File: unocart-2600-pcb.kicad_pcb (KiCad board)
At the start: 2 copper layers, 41.3 x 47.6 mm, 19 parts, among them J1 Conn_02x12_Counter_Clockwise, J2 Micro_SD_Card, J3 Conn_02x03_Odd_Even, J4 Conn_01x03, U1 STM32F407VGTx, U2 MIC5504-3.3YM5

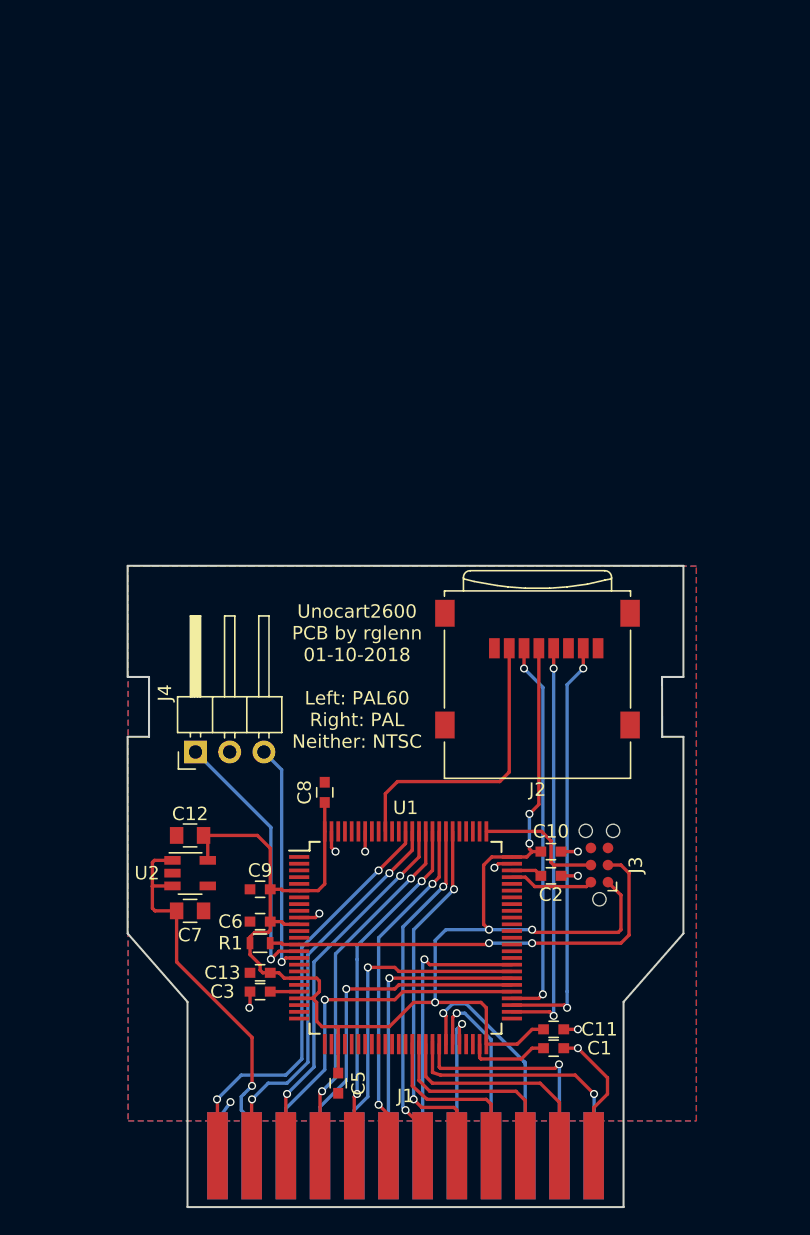
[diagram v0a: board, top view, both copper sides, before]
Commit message: Updating schematic to latest KiCAD libraries Updating PCB to add pull-up resistor on SD card DO Changing to TF-01A push/push MicroSD card socket Updating PCB size to allow a card removal slot on the cartridge body Moving parts to not conflict with internal cartridge face plate Moving PAL60/PAL jumper to solder bridges (I'm doing NTSC, I don't really care about PAL anyways)
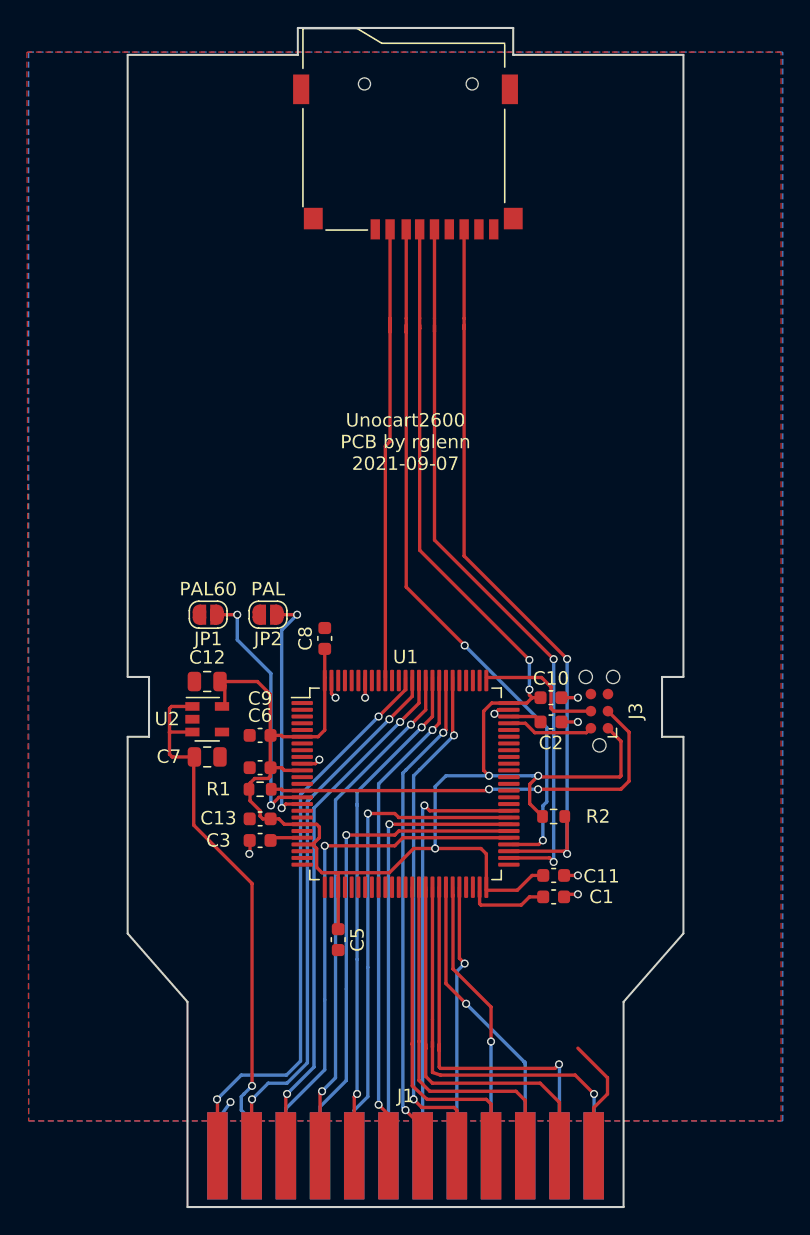
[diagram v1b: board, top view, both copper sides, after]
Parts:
- removed J4: Conn_01x03, Pin_Headers:Pin_Header_Angled_1x03_Pitch2.54mm
- added JP1: PAL60, Jumper:SolderJumper-2_P1.3mm_Open_RoundedPad1.0x1.5mm, F.Cu at (85.3, 56.0)
- added JP2: PAL, Jumper:SolderJumper-2_P1.3mm_Open_RoundedPad1.0x1.5mm, F.Cu at (89.8, 56.0)
- added R2: 10K, Resistor_SMD:R_0603_1608Metric, F.Cu at (111.0, 71.0)
- C1, C10, C11, C13, C2, C3, C5, C6, C8, C9: footprint Capacitors_SMD:C_0603 -> Capacitor_SMD:C_0603_1608Metric
- C12, C7: footprint Capacitors_SMD:C_0805 -> Capacitor_SMD:C_0805_2012Metric
- J2: footprint Connect:microSD_Card_Receptacle_Wuerth_693072010801 -> unocart-2600:microSD_HRO_TF_01A
- J3: footprint Connect:Tag-Connect_TC2030-IDC-NL -> Connector:Tag-Connect_TC2030-IDC-NL_2x03_P1.27mm_Vertical
- R1: footprint Resistors_SMD:R_0603 -> Resistor_SMD:R_0603_1608Metric
- U1: footprint Housings_QFP:LQFP-100_14x14mm_Pitch0.5mm -> Package_QFP:LQFP-100_14x14mm_P0.5mm
- U2: footprint TO_SOT_Packages_SMD:TSOT-23-5 -> Package_TO_SOT_SMD:SOT-23-5
- moved J2 42.4 mm to (100.0, 19.9), turned to 180 degrees
- moved C12 11.5 mm to (85.3, 61.0)
- moved C7 11.5 mm to (85.3, 66.6)
- moved U2 11.5 mm to (85.3, 63.8)
- moved C2 11.4 mm to (110.8, 64.0)
- moved C9 11.4 mm to (89.2, 65.0)
- moved R1 11.4 mm to (89.2, 69.0)
- moved U1 11.4 mm to (100.0, 68.6)
- moved C8 11.4 mm to (94.0, 57.8)
- moved C10 11.4 mm to (110.8, 62.2)
- moved C11 11.4 mm to (111.0, 75.4)
- moved C13 11.4 mm to (89.2, 71.2)
- moved C6 11.4 mm to (89.2, 67.4)
- moved J3 11.4 mm to (114.4, 63.2)
- moved C1 11.2 mm to (111.0, 77.0)
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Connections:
- J2 pad 1: (no net) -> Net-(J2-Pad1)
- J2 pad 8: (no net) -> Net-(J2-Pad8)
- J3 pad 6: (no net) -> Net-(J3-Pad6)
- U1 pad 1: (no net) -> Net-(U1-Pad1)
- U1 pad 12: (no net) -> Net-(U1-Pad12)
- U1 pad 13: (no net) -> Net-(U1-Pad13)
- U1 pad 17: (no net) -> Net-(U1-Pad17)
- U1 pad 18: (no net) -> Net-(U1-Pad18)
- U1 pad 2: (no net) -> Net-(U1-Pad2)
- U1 pad 23: (no net) -> Net-(U1-Pad23)
- U1 pad 24: (no net) -> Net-(U1-Pad24)
- U1 pad 25: (no net) -> Net-(U1-Pad25)
- U1 pad 26: (no net) -> Net-(U1-Pad26)
- U1 pad 29: (no net) -> Net-(U1-Pad29)
- U1 pad 3: (no net) -> Net-(U1-Pad3)
- U1 pad 30: (no net) -> Net-(U1-Pad30)
- U1 pad 31: (no net) -> Net-(U1-Pad31)
- U1 pad 32: (no net) -> Net-(U1-Pad32)
- U1 pad 33: (no net) -> Net-(U1-Pad33)
- U1 pad 34: (no net) -> Net-(U1-Pad34)
- U1 pad 35: (no net) -> Net-(U1-Pad35)
- U1 pad 36: (no net) -> Net-(U1-Pad36)
- U1 pad 37: (no net) -> Net-(U1-Pad37)
- U1 pad 38: (no net) -> Net-(U1-Pad38)
- U1 pad 4: (no net) -> Net-(U1-Pad4)
- U1 pad 47: (no net) -> Net-(U1-Pad47)
- U1 pad 48: (no net) -> Net-(U1-Pad48)
- U1 pad 5: (no net) -> Net-(U1-Pad5)
- U1 pad 51: (no net) -> Net-(U1-Pad51)
- U1 pad 60: (no net) -> Net-(U1-Pad60)
- U1 pad 61: (no net) -> Net-(U1-Pad61)
- U1 pad 62: (no net) -> Net-(U1-Pad62)
- U1 pad 63: (no net) -> Net-(U1-Pad63)
- U1 pad 64: (no net) -> Net-(U1-Pad64)
- U1 pad 65: (no net) -> Net-(U1-Pad65)
- U1 pad 66: (no net) -> Net-(U1-Pad66)
- U1 pad 67: (no net) -> Net-(U1-Pad67)
- U1 pad 68: (no net) -> Net-(U1-Pad68)
- U1 pad 69: (no net) -> Net-(U1-Pad69)
- U1 pad 7: (no net) -> Net-(U1-Pad7)
- U1 pad 70: (no net) -> Net-(U1-Pad70)
- U1 pad 71: (no net) -> Net-(U1-Pad71)
- U1 pad 77: (no net) -> Net-(U1-Pad77)
- U1 pad 78: (no net) -> Net-(U1-Pad78)
- U1 pad 79: (no net) -> Net-(U1-Pad79)
- U1 pad 8: (no net) -> Net-(U1-Pad8)
- U1 pad 80: (no net) -> Net-(U1-Pad80)
- U1 pad 89: (no net) -> Net-(U1-Pad89)
- U1 pad 9: (no net) -> Net-(U1-Pad9)
- U1 pad 90: (no net) -> Net-(U1-Pad90)
- U1 pad 92: (no net) -> Net-(U1-Pad92)
- U1 pad 93: (no net) -> Net-(U1-Pad93)
- U1 pad 95: (no net) -> Net-(U1-Pad95)
- U1 pad 96: (no net) -> Net-(U1-Pad96)
- U1 pad 97: (no net) -> Net-(U1-Pad97)
- U1 pad 98: (no net) -> Net-(U1-Pad98)
- U2 pad 4: (no net) -> Net-(U2-Pad4)
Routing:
- net +3V3: track 112.2 -> 138.6 mm
- net /DO: track 31.4 -> 56.8 mm
- net /DI: track 28.7 -> 52.8 mm
- net /SCK: track 30.5 -> 54.3 mm
- net /CS: track 21.9 -> 34.7 mm
- net /D4: track 17.6 -> 29.7 mm
- net /D2: track 17.1 -> 29.1 mm
- net /D3: track 19.5 -> 31.4 mm
- net /A6: track 29.9 -> 41.7 mm
- net /D0: track 13.4 -> 25.1 mm
- net /A3: track 26.5 -> 38.0 mm
- net /A7: track 31.8 -> 43.3 mm
- net /D1: track 15.5 -> 27.0 mm
- net /A11: track 25.2 -> 36.7 mm
- net /A9: track 25.6 -> 37.1 mm
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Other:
- board size 41.3 x 47.6 mm -> 41.3 x 87.6 mm
- board text added: "Unocart2600 PCB by rglenn 2021-09-07"
- board text removed: "Unocart2600 PCB by rglenn 01-10-2018 Left: PAL60 Right: PAL Neither: NTSC"

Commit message: Shortening the PCB by 0.5mm after a test fit of a 1:1 printout in the case
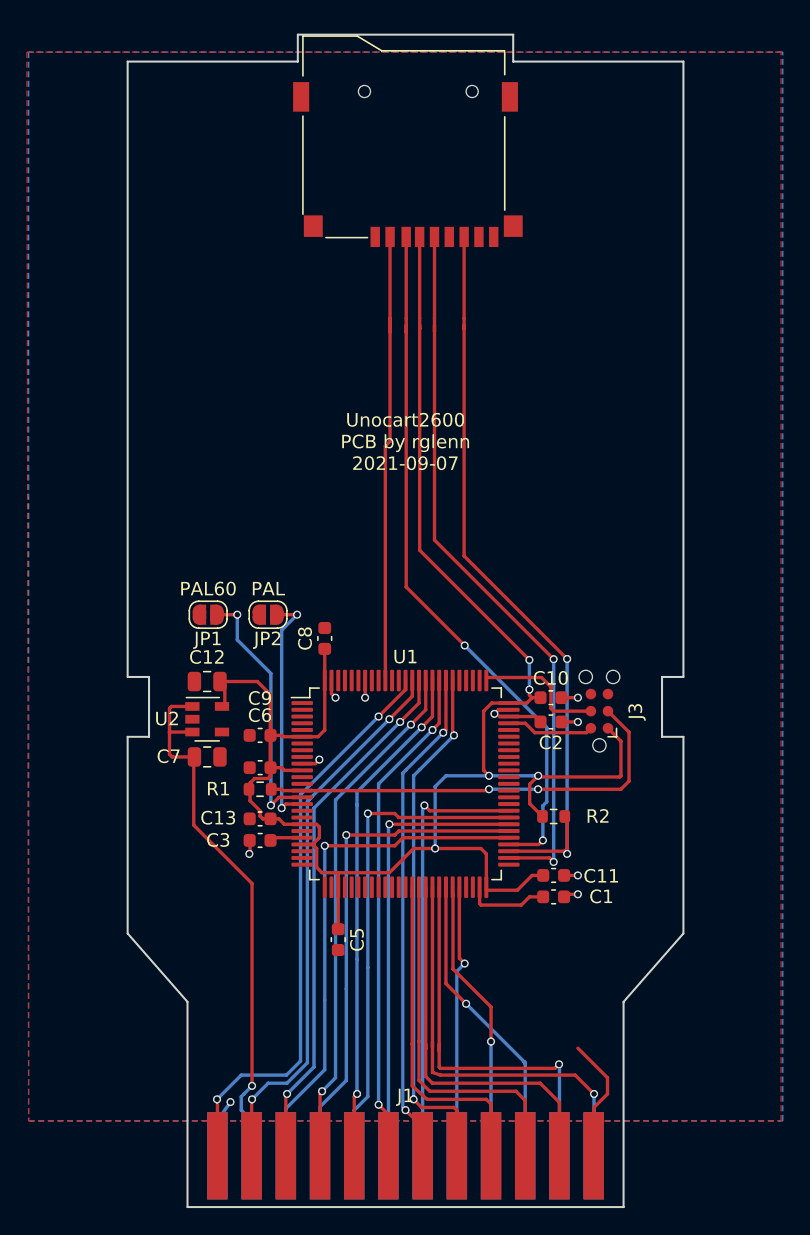
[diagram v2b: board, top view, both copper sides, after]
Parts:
- moved J2 0.56 mm to (100.0, 20.5)
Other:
- board size 41.3 x 87.6 mm -> 41.3 x 87.1 mm

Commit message: DRC clean, added license text to schematic and PCB
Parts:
- added REF**: OSHW-Symbol_6.7x6mm_SilkScreen, Symbol:OSHW-Symbol_6.7x6mm_SilkScreen, F.Cu at (100.0, 35.0)
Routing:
- net /D6: track 21.3 -> 22.6 mm
- net GND: track 25.6 -> 26.7 mm
- net +3V3: track 138.6 -> 139.3 mm
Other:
- board text added: "Copyright Randy Glenn 2021. This documentation describes Open Hardware and is licensed under the CERN OHL v. 1.2. You may redistribute and modify this documentation under the terms of the CERN OHL v.1.2. (http://ohwr.org/cernohl). This documentation is distributed WITHOUT ANY EXPRESS OR IMPLIED WARRANTY, INCLUDING OF MERCHANTABILITY, SATISFACTORY QUALITY AND FITNESS FOR A PARTICULAR PURPOSE. Plea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"
